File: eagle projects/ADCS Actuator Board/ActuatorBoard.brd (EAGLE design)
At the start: 91 x 91 mm, 228 parts, among them J11 TE_1-84953-1, J2 TE_1-84953-1, J4 TE_1-84953-1, J5 TE-1734829-3, U1 SIP2100DY-T1-GE3, U10 LM2917MX/NOPB, U12 TSV991AILT, U13 LM2917MX/NOPB, U14 ADS7841E_2K5, U16 DRV10970_MOTOR_DRIVERDRV10970, U17 LM2917MX/NOPB, U19 TSV991AILT, U2 SIP2100DY-T1-GE3, U20 ADS7841E_2K5, U3 SIP2100DY-T1-GE3, U6 DRV10970_MOTOR_DRIVERDRV10970, U7 DRV10970_MOTOR_DRIVERDRV10970, U8 TSV991AILT, U9 ADS7841E_2K5

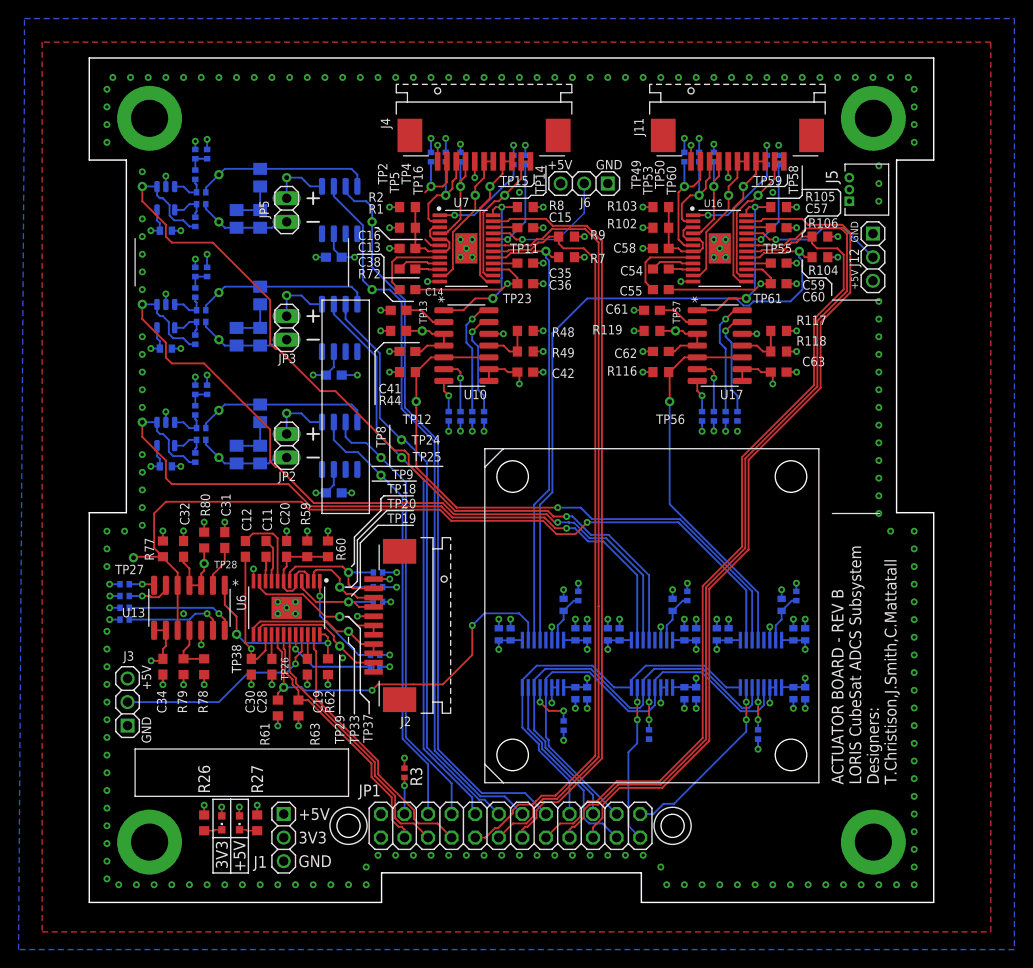
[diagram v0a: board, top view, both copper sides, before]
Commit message: stitching vias and silkscreen and fixed reversed totem pole driver (oops)
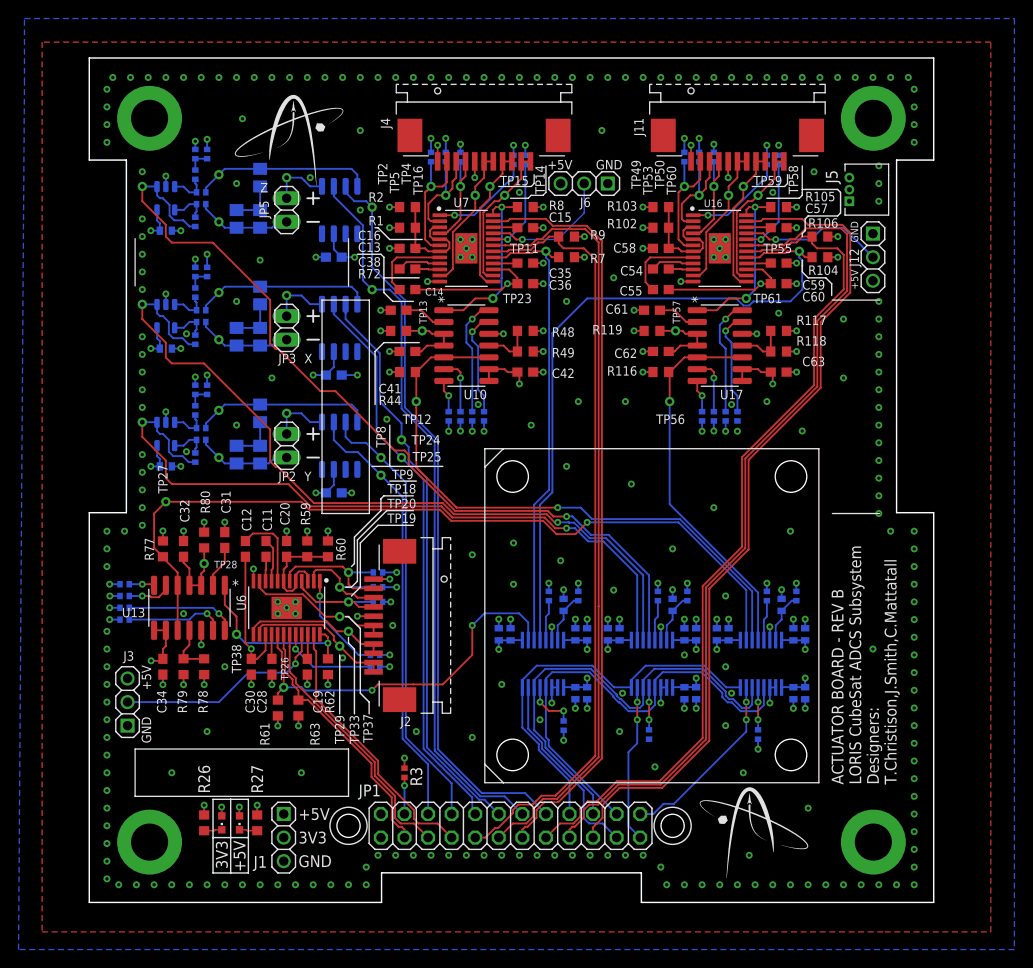
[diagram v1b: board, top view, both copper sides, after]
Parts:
- added R13, R14, R4: 5.1M, rcl:R0402
- moved TP27 6.97 mm to (8.26, 43.2)
- moved TP47 1.59 mm to (30.5, 74.9)
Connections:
- net GND: now also R13.2, R14.2, R4.2
- net N$26: now also R14.1
- net N$46: now also R13.1
- net N$60: now also R4.1
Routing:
- net X_HALL_C: track 9.57 -> 14.6 mm
- net N$60: track 0.00 -> 4.38 mm
- net N$46: track 0.00 -> 4.38 mm
- net N$26: track 0.00 -> 4.38 mm
- net RW_Z_SPD: track 91.6 -> 88.5 mm
- net GND: track 120.4 -> 123.0 mm, vias 300 -> 359
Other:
- board text added: "X"
- board text added: "Y"
- board text added: "Z"

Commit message: done
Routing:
- net +3V3: track 65.4 -> 63.0 mm
- net +5V: track 93.0 -> 91.9 mm
- net MAG_X_RIN: track 48.3 -> 47.2 mm
- net MAG_Y_FIN: track 63.1 -> 62.1 mm
- net MAG_X_FIN: track 48.6 -> 47.9 mm

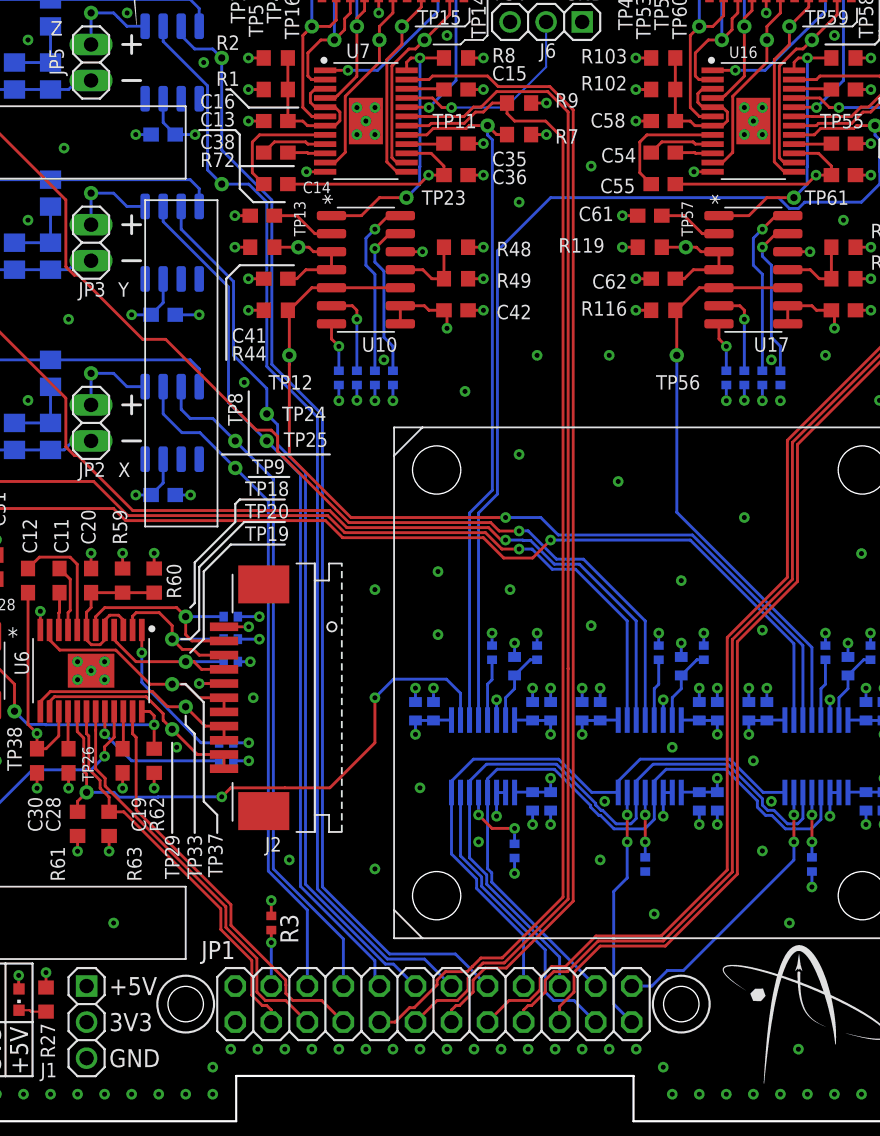
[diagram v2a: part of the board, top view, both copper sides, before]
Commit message: Partially Replaced Connectors on Actuator
Will finish soon
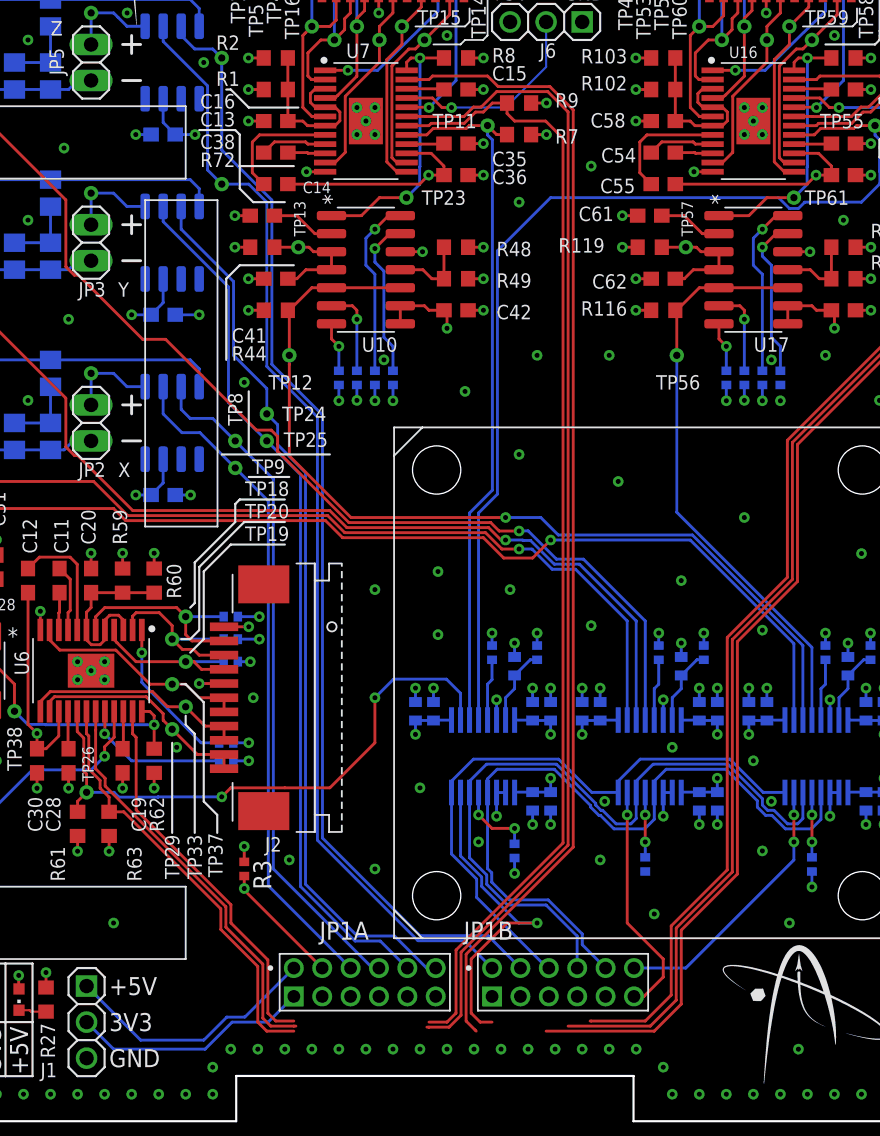
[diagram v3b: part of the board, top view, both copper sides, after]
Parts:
- removed JP1: (no value), pinhead:2X12
- added JP1A, JP1B: 832-10-012-10-005000, 832-10-012-10-005000:832-10-012-10-005000
- moved R3 4.26 mm to (32.1, 17.8)
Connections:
- net !CS!_CURR_SENSE_MTQR: now also JP1B.11; no longer JP1.23
- net !CS!_CURR_SENSE_RW: now also JP1B.9; no longer JP1.21
- net !CS!_SPD_SENSE_RW: now also JP1B.12; no longer JP1.24
- net +3V3: now also JP1A.1; no longer JP1.1
- net +5V: now also JP1A.2; no longer JP1.2
- net MAG_X_FIN: now also JP1A.8; no longer JP1.8
- net MAG_X_RIN: now also JP1A.6; no longer JP1.6
- net MAG_Y_FIN: now also JP1A.12; no longer JP1.12
- net MAG_Y_RIN: now also JP1A.10; no longer JP1.10
- net MAG_Z_FIN: now also JP1B.4; no longer JP1.16
- net MAG_Z_RIN: now also JP1B.2; no longer JP1.14
- net N$1: now also JP1A.4; no longer JP1.4
- net RW_X_DIR: now also JP1B.1; no longer JP1.13
- net RW_X_LOCK: now also JP1A.9; no longer JP1.9
- net RW_X_SPEED_CTRL: now also JP1A.11; no longer JP1.11
- net RW_Y_DIR: now also JP1B.7; no longer JP1.19
- net RW_Y_LOCK: now also JP1B.3; no longer JP1.15
- net RW_Y_SPEED_CTRL: now also JP1B.5; no longer JP1.17
- net RW_Z_DIR: now also JP1A.7; no longer JP1.7
- net RW_Z_LOCK: now also JP1A.3; no longer JP1.3
- net RW_Z_SPEED_CTRL: now also JP1A.5; no longer JP1.5
- net UCB0_SPI_CLK: now also JP1B.6; no longer JP1.18
- net UCB0_SPI_MISO: now also JP1B.10; no longer JP1.22
- net UCB0_SPI_MOSI: now also JP1B.8; no longer JP1.20
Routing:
- net +5V: track 91.9 -> 110.2 mm
- net +3V3: track 63.0 -> 79.9 mm
- net RW_Y_LOCK: track 92.6 -> 87.7 mm
- net N$1: track 3.95 -> 8.76 mm
- net RW_X_LOCK: track 83.4 -> 80.1 mm
- net RW_Y_DIR: track 91.3 -> 94.1 mm
- net !CS!_CURR_SENSE_RW: track 21.0 -> 23.5 mm, vias 0 -> 1
- net RW_Z_LOCK: track 28.1 -> 30.3 mm
- net RW_Z_DIR: track 29.2 -> 27.3 mm
- net RW_Y_SPEED_CTRL: track 92.7 -> 91.6 mm
- net MAG_Y_FIN: track 62.1 -> 63.0 mm
- net UCB0_SPI_MOSI: track 50.1 -> 51.0 mm
- net RW_X_SPEED_CTRL: track 83.0 -> 82.2 mm
- net !CS!_SPD_SENSE_RW: track 19.9 -> 19.2 mm
- net UCB0_SPI_MISO: track 50.8 -> 51.4 mm
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
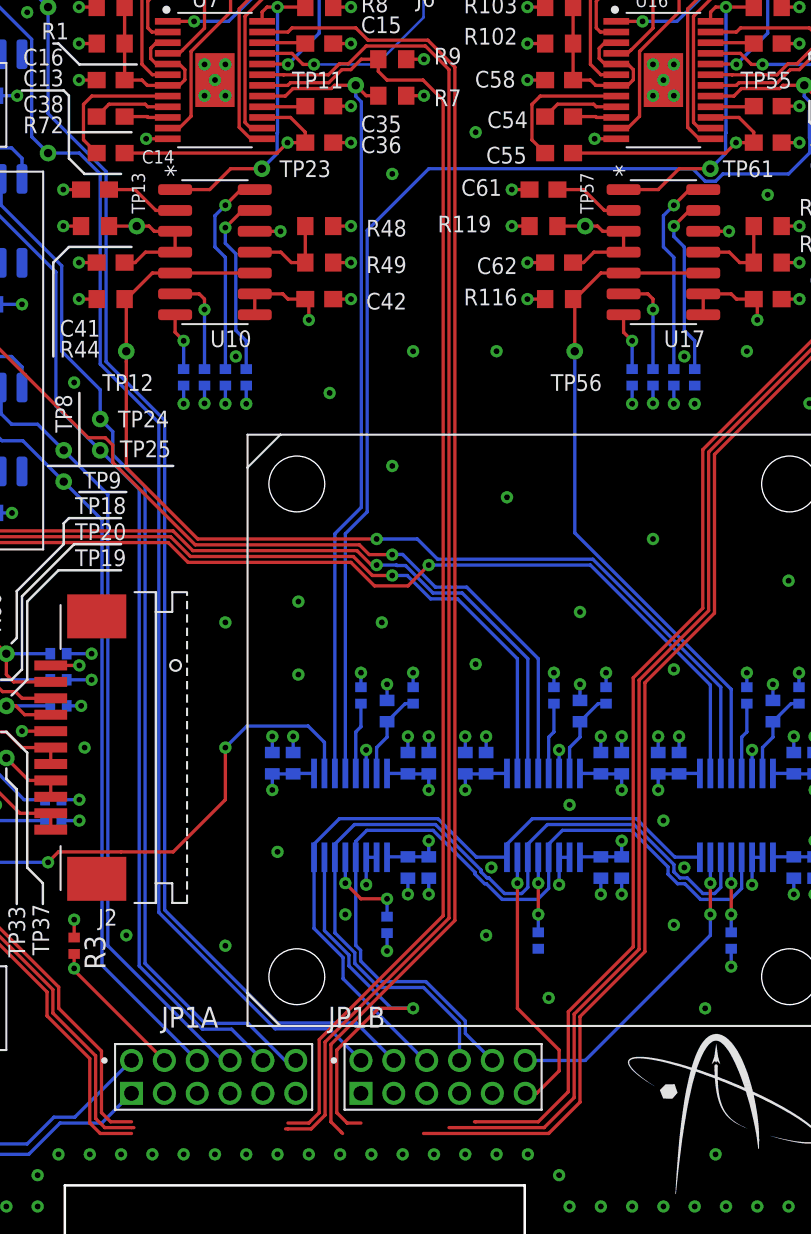
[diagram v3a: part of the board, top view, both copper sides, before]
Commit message: Arranged 12x2 Connectors on Motherboard and Actuator Board
Unfinished, needs cleanup
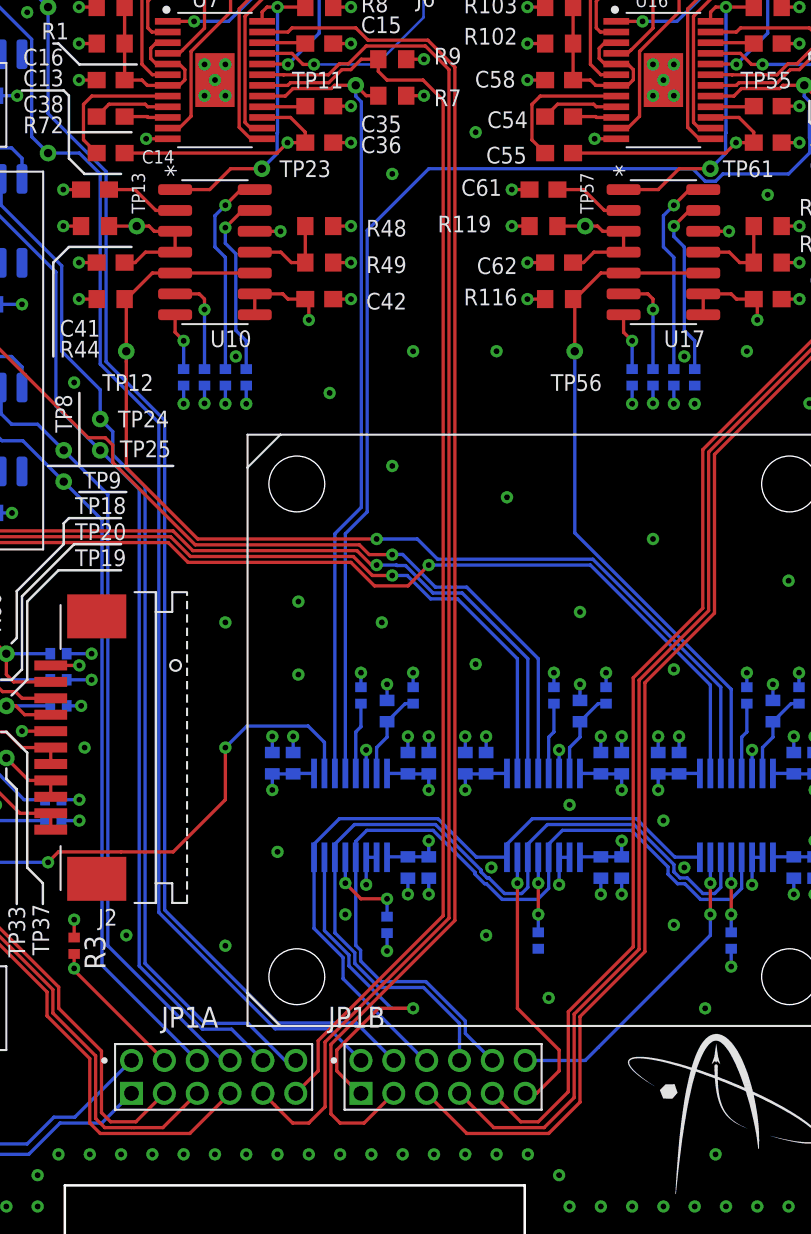
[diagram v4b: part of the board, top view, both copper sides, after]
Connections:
- net !CS!_CURR_SENSE_RW: now also JP1B.1; no longer JP1B.9
- net RW_X_DIR: now also JP1B.3; no longer JP1B.1
- net RW_X_LOCK: now also JP1A.11; no longer JP1A.9
- net RW_X_SPEED_CTRL: now also JP1A.9; no longer JP1A.11
- net RW_Y_DIR: now also JP1B.5; no longer JP1B.7
- net RW_Y_LOCK: now also JP1B.9; no longer JP1B.3
- net RW_Y_SPEED_CTRL: now also JP1B.7; no longer JP1B.5
- net RW_Z_DIR: now also JP1A.3; no longer JP1A.7
- net RW_Z_LOCK: now also JP1A.7; no longer JP1A.3
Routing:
- net RW_Z_LOCK: track 30.3 -> 37.3 mm
- net RW_Z_SPEED_CTRL: track 29.1 -> 33.8 mm
- net RW_X_DIR: track 81.3 -> 84.5 mm
- net RW_X_LOCK: track 80.1 -> 77.3 mm
- net RW_Z_DIR: track 27.3 -> 30.0 mm
- net !CS!_CURR_SENSE_RW: track 23.5 -> 21.2 mm
- net RW_X_SPEED_CTRL: track 82.2 -> 83.9 mm
- net RW_Y_DIR: track 94.1 -> 94.9 mm

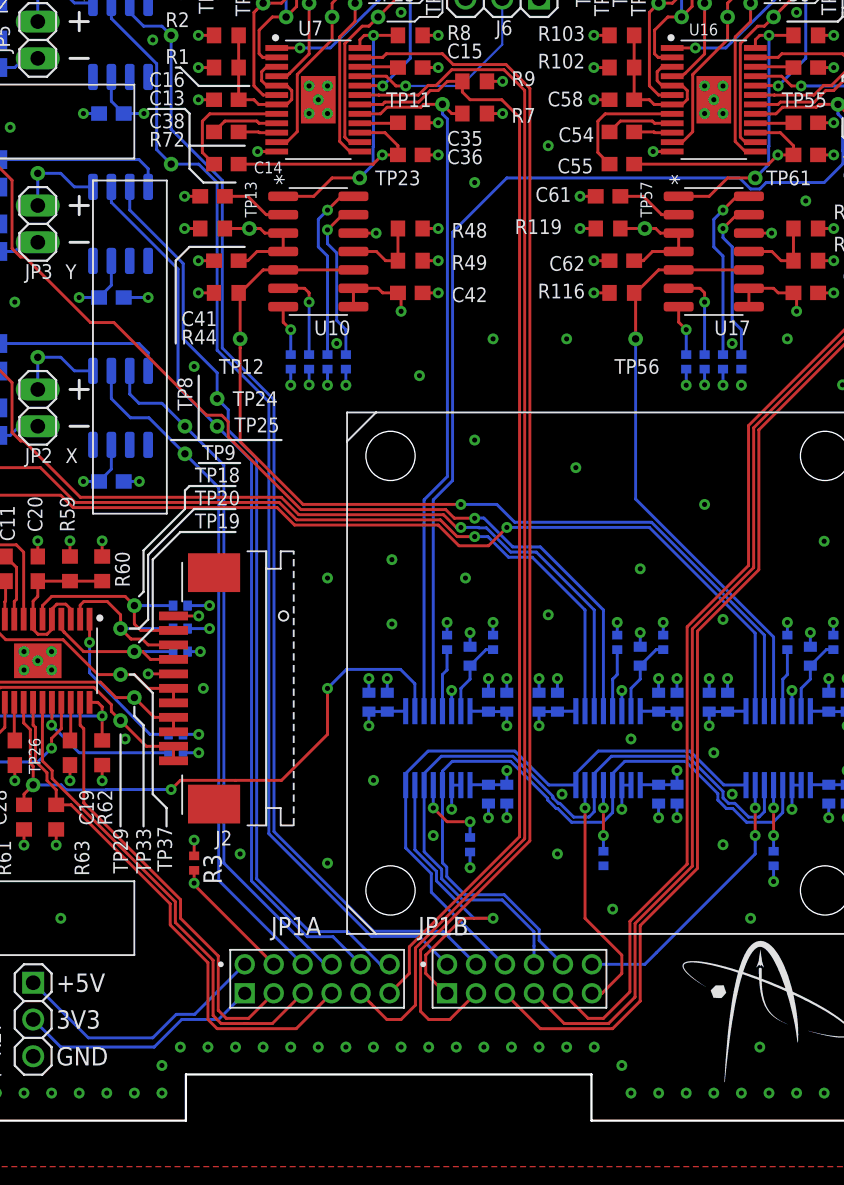
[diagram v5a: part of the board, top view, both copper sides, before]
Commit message: Centered connector on Actuator Board
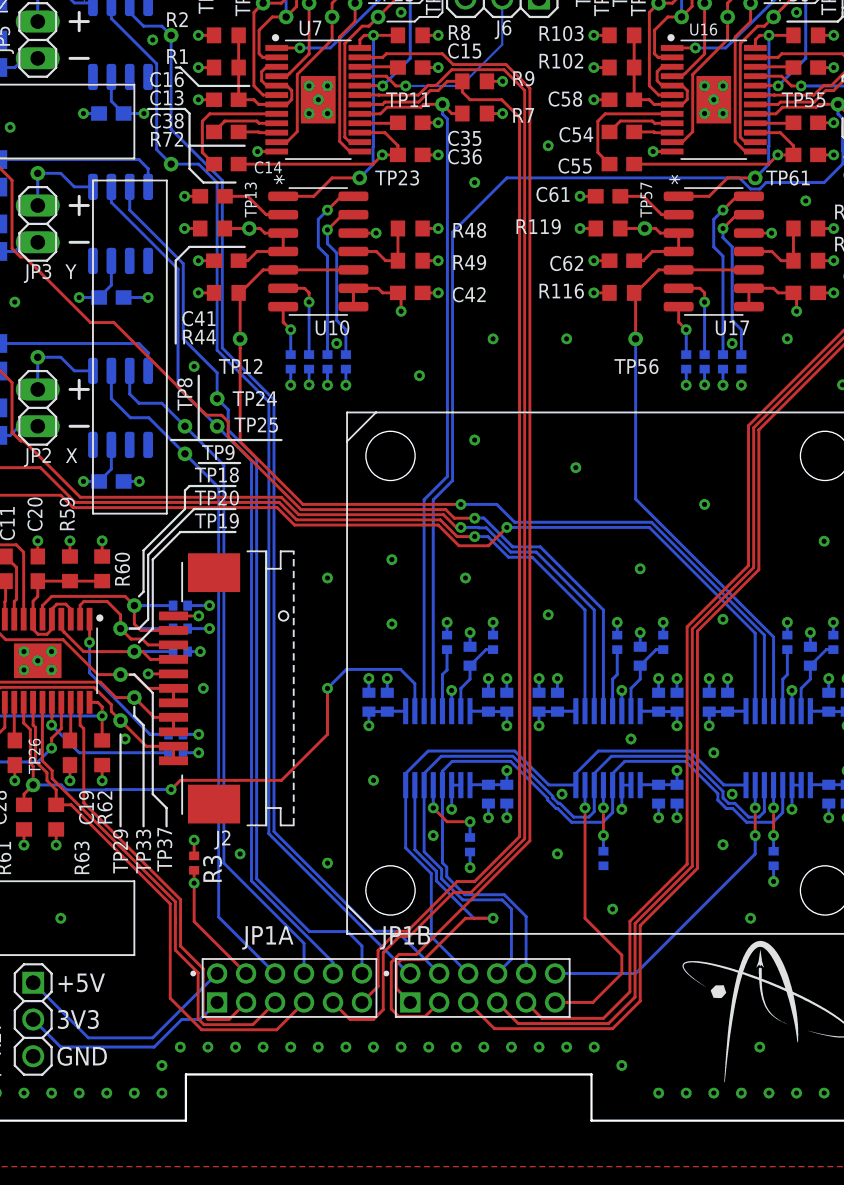
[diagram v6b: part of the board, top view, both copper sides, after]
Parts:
- moved JP1B 2.62 mm to (47.0, 10.2)
- moved JP1A 2.01 mm to (33.7, 10.2)
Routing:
- net !CS!_CURR_SENSE_MTQR: track 16.7 -> 19.5 mm
- net !CS!_SPD_SENSE_RW: track 19.2 -> 22.0 mm
- net RW_X_LOCK: track 77.3 -> 79.9 mm
- net RW_Y_DIR: track 94.9 -> 97.2 mm
- net MAG_Z_RIN: track 79.0 -> 76.7 mm
- net RW_Y_SPEED_CTRL: track 91.9 -> 94.1 mm
- net RW_Y_LOCK: track 87.3 -> 89.6 mm
- net MAG_Z_FIN: track 79.8 -> 77.5 mm
- net +5V: track 110.2 -> 108.0 mm
- net +3V3: track 79.9 -> 77.8 mm
- net !CS!_CURR_SENSE_RW: track 21.2 -> 23.2 mm
- net RW_X_SPEED_CTRL: track 83.9 -> 85.6 mm
- net RW_Z_LOCK: track 37.3 -> 35.9 mm
- net RW_Z_SPEED_CTRL: track 33.8 -> 32.4 mm
- net RW_Z_DIR: track 30.0 -> 28.7 mm
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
